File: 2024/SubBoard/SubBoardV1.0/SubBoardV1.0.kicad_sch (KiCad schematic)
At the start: 18 parts, among them J1 Conn_01x02_Socket, J10 Conn_01x02_Socket, J11 Conn_01x03_Socket, J12 Conn_01x02_Socket, J13 Conn_01x02_Socket, J14 Conn_01x06_Socket, J15 Conn_01x06_Socket, J16 Conn_01x12_Socket, J2 Conn_01x02_Socket, J3 Conn_01x02_Socket, J4 Conn_01x02_Socket, J5 Conn_01x02_Socket, J6 Conn_01x02_Socket, J7 Conn_01x02_Socket, J8 Conn_01x02_Socket, J9 Conn_01x02_Socket

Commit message: add Kick&Sub
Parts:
- removed J16: Conn_01x12_Socket, Connector_PinHeader_2.54mm:PinHeader_2x06_P2.54mm_Vertical, symbol Connector:Conn_01x12_Socket
- added J17: Conn_01x14_Socket, Connector_PinHeader_2.54mm:PinHeader_2x07_P2.54mm_Vertical, symbol Connector:Conn_01x14_Socket
- added R1: 20k, Resistor_SMD:R_0603_1608Metric, symbol Device:R
- added R7: 470, Resistor_SMD:R_0603_1608Metric, symbol Device:R
- C1, C2: value C -> 1500u; footprint Capacitor_SMD:CP_Elec_10x10 -> Capacitor_THT:CP_Radial_D12.5mm_P5.00mm
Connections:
- net +15V: now also J14.1 (Pin_1), J15.1 (Pin_1), J17.1 (Pin_1), J17.2 (Pin_2), J17.3 (Pin_3), J17.4 (Pin_4); no longer J14.2 (Pin_2), J15.2 (Pin_2)
- net +3.3V: now also J14.4 (Pin_4), J15.4 (Pin_4), J17.8 (Pin_8); no longer J13.2 (Pin_2), J14.3 (Pin_3), J15.3 (Pin_3)
- net +5V: now also J12.1 (Pin_1), J14.3 (Pin_3), J15.3 (Pin_3), J17.6 (Pin_6), R7.2; no longer J14.4 (Pin_4), J15.4 (Pin_4)
- net CANH: now also J17.9 (Pin_9)
- net CANL: now also J17.10 (Pin_10)
- net GND: now also J13.2 (Pin_2), J14.2 (Pin_2), J15.2 (Pin_2), J17.11 (Pin_11), J17.12 (Pin_12), J17.13 (Pin_13), J17.14 (Pin_14), R1.1; no longer J12.1 (Pin_1), J13.1 (Pin_1), J14.1 (Pin_1), J15.1 (Pin_1)
- net SIGNAL renamed DRI_SIGNAL
- net DRI_SIGNAL: now also J17.5 (Pin_5); no longer J12.2 (Pin_2)
- new net: J13.1 (Pin_1), R7.1
- new net TR_SIGNAL: J12.2 (Pin_2), J17.7 (Pin_7), R1.2

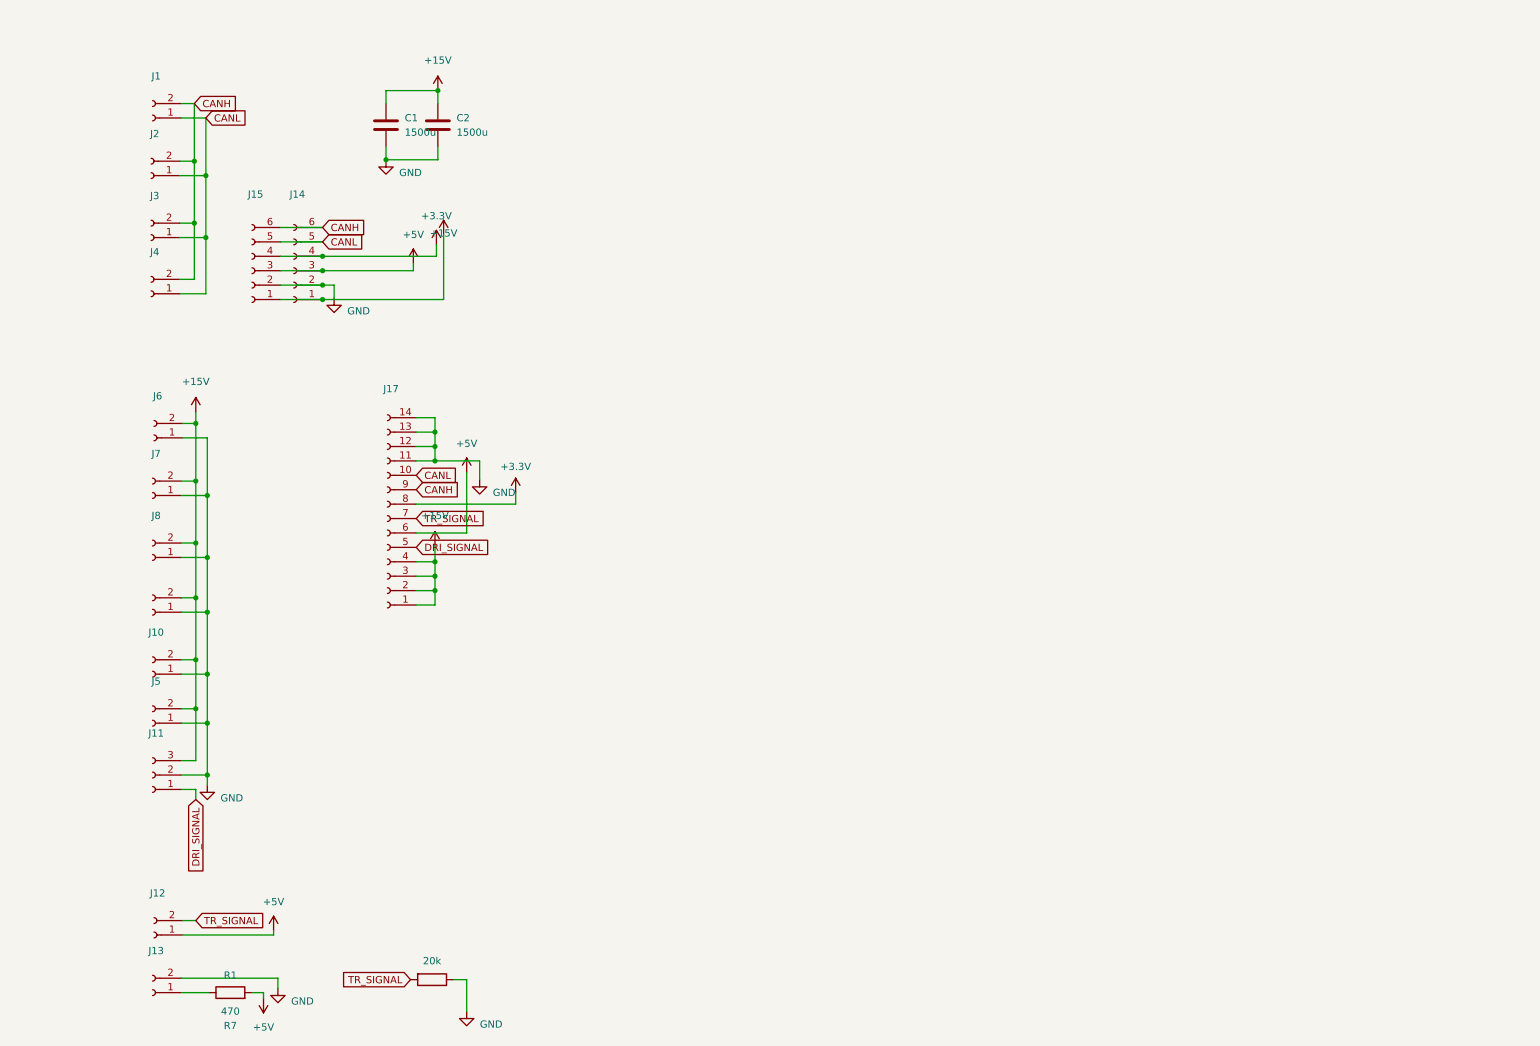
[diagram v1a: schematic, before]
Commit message: improved schematic readability
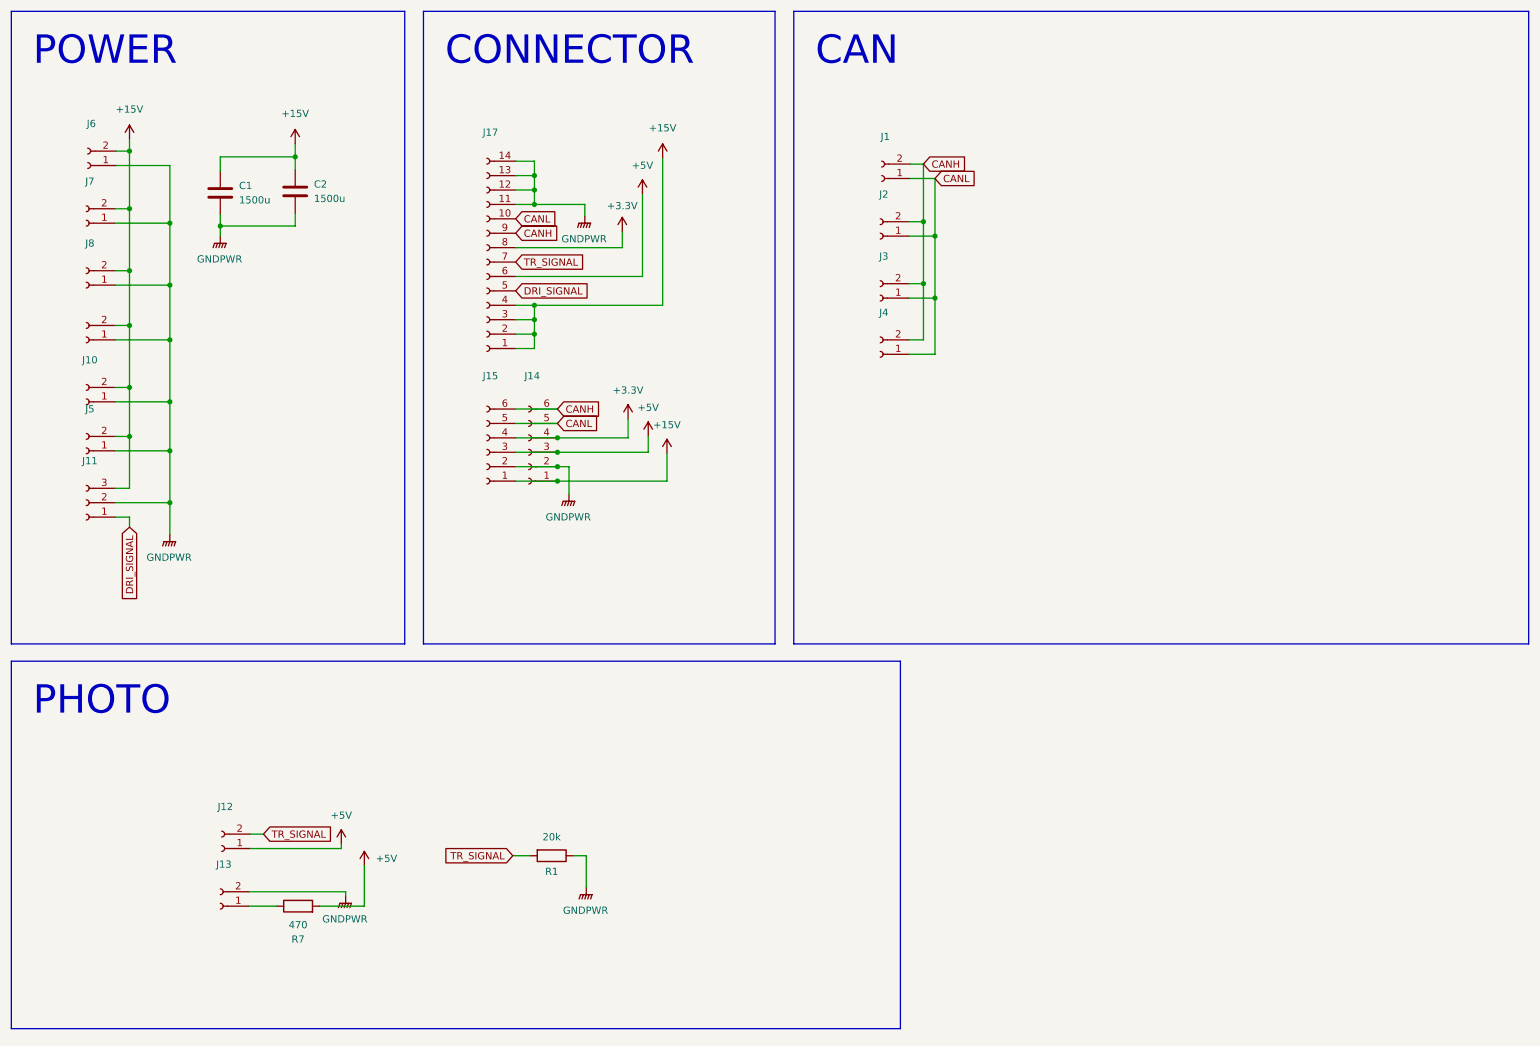
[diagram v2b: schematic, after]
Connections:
- net GND renamed GNDPWR
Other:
- company: (none) -> Ri-oneSSL
- title: (none) -> SubBoardVer1.0
- moved on the sheet: C1, C2, J1, J10, J11, J12, J13, J14, J15, J17, J2, J3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
